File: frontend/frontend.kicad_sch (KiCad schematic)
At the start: 46 parts, among them Q1 T2N7002AK,LM, Q2 NX3008PBK,215, Q3 NX3008PBK,215, Q4 T2N7002AK,LM, Q5 NX3008PBK,215, Q6 T2N7002AK,LM, U1 ADS1291/2, U2 KC2016Z2

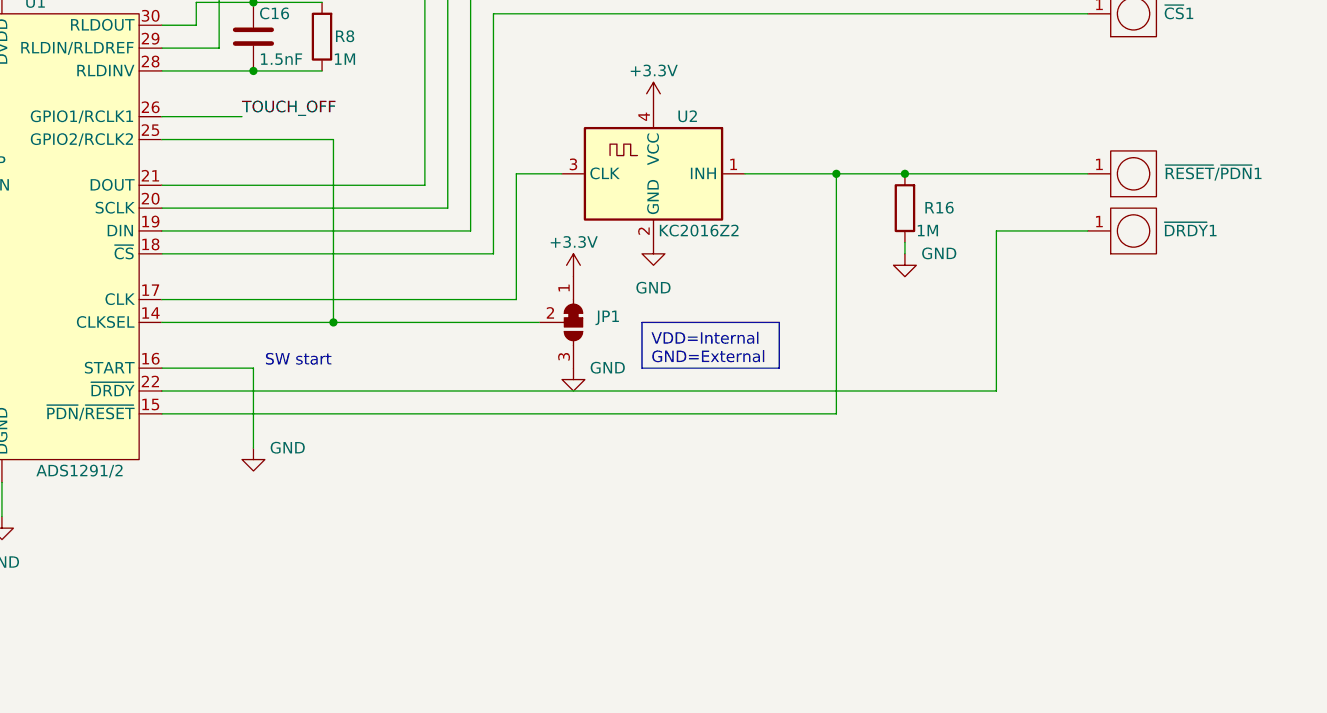
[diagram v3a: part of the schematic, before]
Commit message: Fix #8: add input to disable oscillator
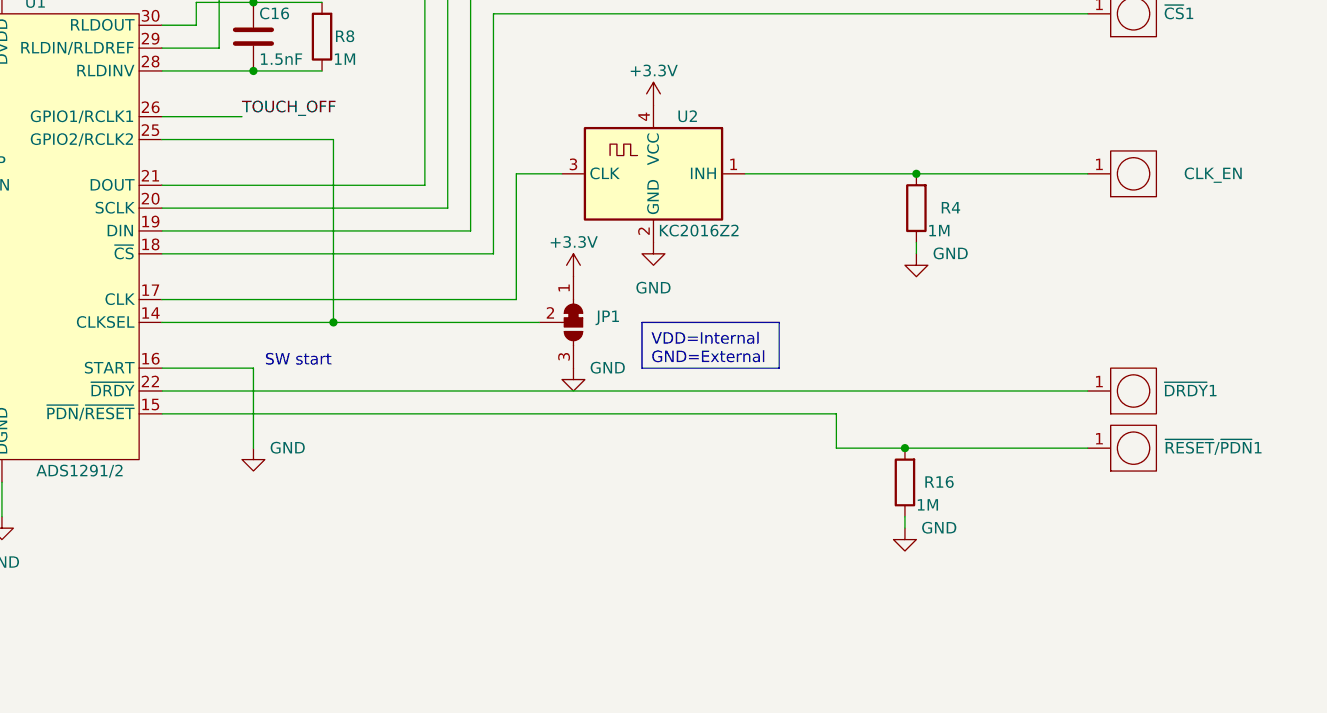
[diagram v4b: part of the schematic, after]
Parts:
- added CLK_EN: ~, frontend_parts:PAD, symbol frontend_parts:PAD
- added R4: 1M, Resistor_SMD:R_0603_1608Metric, symbol Device:R
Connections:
- net GND: now also R4.1
- net at R16.2, U1.15 (~{PDN}/~{RESET}), ~{RESET}/~{PDN}1.1: no longer U2.1 (INH)
- new net: CLK_EN.1, R4.2, U2.1 (INH)
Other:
- moved on the sheet: R16, ~{DRDY}1, ~{RESET}/~{PDN}1
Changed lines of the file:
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@@
   (junction (at 50.8 21.59) (diameter 0) (color 0 0 0 0)
   )
+  (junction (at 245.11 115.57) (diameter 0) (color 0 0 0 0)
+  )
   (junction (at 73.66 35.56) (diameter 0) (color 0 0 0 0)
   )
@@
   (junction (at 171.45 96.52) (diameter 0) (color 0 0 0 0)
   )
-  (junction (at 243.84 115.57) (diameter 0) (color 0 0 0 0)
-  )
   (junction (at 171.45 104.14) (diameter 0) (color 0 0 0 0)
   )
-  (junction (at 236.22 115.57) (diameter 0) (color 0 0 0 0)
-  )
   (junction (at 121.92 106.68) (diameter 0) (color 0 0 0 0)
   )
   (junction (at 156.21 87.63) (diameter 0) (color 0 0 0 0)
   )
+  (junction (at 243.84 146.05) (diameter 0) (color 0 0 0 0)
+  )
   (junction (at 52.07 67.31) (diameter 0) (color 0 0 0 0)
   )
@@
     (stroke (width 0) (type default))
   )
+  (wire (pts (xy 226.06 115.57) (xy 245.11 115.57))
+    (stroke (width 0) (type default))
+  )
   (wire (pts (xy 39.37 72.39) (xy 44.45 72.39))
     (stroke (width 0) (type default))
   )
-  (wire (pts (xy 236.22 115.57) (xy 243.84 115.57))
+  (wire (pts (xy 236.22 146.05) (xy 243.84 146.05))
     (stroke (width 0) (type default))
   )
@@
     (stroke (width 0) (type default))
   )
-  (wire (pts (xy 254 139.7) (xy 254 121.92))
-    (stroke (width 0) (type default))
-  )
   (wire (pts (xy 24.13 66.04) (xy 31.75 66.04))
     (stroke (width 0) (type default))
@@
     (stroke (width 0) (type default))
   )
+  (wire (pts (xy 245.11 123.19) (xy 245.11 124.46))
+    (stroke (width 0) (type default))
+  )
   (wire (pts (xy 143.51 149.86) (xy 143.51 153.67))
     (stroke (width 0) (type default))
@@
     (stroke (width 0) (type default))
   )
-  (wire (pts (xy 243.84 115.57) (xy 264.16 115.57))
+  (wire (pts (xy 243.84 146.05) (xy 264.16 146.05))
     (stroke (width 0) (type default))
   )
@@
     (stroke (width 0) (type default))
   )
-  (wire (pts (xy 226.06 115.57) (xy 236.22 115.57))
-    (stroke (width 0) (type default))
-  )
   (wire (pts (xy 57.15 101.6) (xy 125.73 101.6))
     (stroke (width 0) (type default))
@@
     (stroke (width 0) (type default))
   )
-  (wire (pts (xy 236.22 115.57) (xy 236.22 142.24))
+  (wire (pts (xy 236.22 146.05) (xy 236.22 142.24))
     (stroke (width 0) (type default))
   )
@@
     (stroke (width 0) (type default))
   )
-  (wire (pts (xy 254 121.92) (xy 264.16 121.92))
-    (stroke (width 0) (type default))
-  )
   (wire (pts (xy 66.04 40.64) (xy 66.04 44.45))
     (stroke (width 0) (type default))
@@
     (stroke (width 0) (type default))
   )
+  (wire (pts (xy 245.11 115.57) (xy 264.16 115.57))
+    (stroke (width 0) (type default))
+  )
   (wire (pts (xy 55.88 99.06) (xy 125.73 99.06))
     (stroke (width 0) (type default))
@@
     (stroke (width 0) (type default))
   )
-  (wire (pts (xy 243.84 123.19) (xy 243.84 124.46))
+  (wire (pts (xy 243.84 153.67) (xy 243.84 154.94))
     (stroke (width 0) (type default))
   )
@@
     (stroke (width 0) (type default))
   )
-  (wire (pts (xy 161.29 139.7) (xy 254 139.7))
+  (wire (pts (xy 161.29 139.7) (xy 264.16 139.7))
     (stroke (width 0) (type default))
   )
@@
     )
   )
-  (symbol (lib_id "frontend_parts:PAD") (at 269.24 121.92 0) (mirror x) (unit 1)
-    (in_bom yes) (on_board yes) (dnp no)
-    (property "Reference" "~{DRDY}1" (at 275.59 121.92 0)
-      (effects (font (size 1.27 1.27)))
-    )
-    (property "Value" "~" (at 264.16 124.46 0)
-      (effects (font (size 1.27 1.27)))
-    )
-    (property "Footprint" "frontend_parts:PAD" (at 264.16 124.46 0)
-      (effects (font (size 1.27 1.27)) hide)
-    )
-    (property "Datasheet" "" (at 264.16 124.46 0)
+  (symbol (lib_id "frontend_parts:PAD") (at 269.24 139.7 0) (mirror x) (unit 1)
+    (in_bom yes) (on_board yes) (dnp no)
+    (property "Reference" "~{DRDY}1" (at 275.59 139.7 0)
+      (effects (font (size 1.27 1.27)))
+    )
+    (property "Value" "~" (at 264.16 142.24 0)
+      (effects (font (size 1.27 1.27)))
+    )
+    (property "Footprint" "frontend_parts:PAD" (at 264.16 142.24 0)
+      (effects (font (size 1.27 1.27)) hide)
+    )
+    (property "Datasheet" "" (at 264.16 142.24 0)
       (effects (font (size 1.27 1.27)) hide)
     )
@@
         (path "/e7afbd42-f5d0-401b-b125-21ade79cd152"
           (reference "R2") (unit 1)
+        )
+      )
+    )
+  )
+  (symbol (lib_id "frontend_parts:PAD") (at 269.24 115.57 0) (mirror x) (unit 1)
+    (in_bom yes) (on_board yes) (dnp no)
+    (property "Reference" "CLK_EN" (at 278.13 115.57 0)
+      (effects (font (size 1.27 1.27)))
+    )
+    (property "Value" "~" (at 264.16 118.11 0)
+      (effects (font (size 1.27 1.27)))
+    )
+    (property "Footprint" "frontend_parts:PAD" (at 264.16 118.11 0)
+      (effects (font (size 1.27 1.27)) hide)
+    )
+    (property "Datasheet" "" (at 264.16 118.11 0)
+      (effects (font (size 1.27 1.27)) hide)
+    )
+    (pin "1")
+    (instances
+      (project "frontend"
+        (path "/e7afbd42-f5d0-401b-b125-21ade79cd152"
+          (reference "CLK_EN") (unit 1)
         )
       )
@@
     )
   )
-  (symbol (lib_id "frontend_parts:PAD") (at 269.24 115.57 0) (mirror x) (unit 1)
-    (in_bom yes) (on_board yes) (dnp no)
-    (property "Reference" "~{RESET}/~{PDN}1" (at 278.13 115.57 0)
-      (effects (font (size 1.27 1.27)))
-    )
-    (property "Value" "~" (at 264.16 118.11 0)
-      (effects (font (size 1.27 1.27)))
-    )
-    (property "Footprint" "frontend_parts:PAD" (at 264.16 118.11 0)
-      (effects (font (size 1.27 1.27)) hide)
-    )
-    (property "Datasheet" "" (at 264.16 118.11 0)
+  (symbol (lib_id "frontend_parts:PAD") (at 269.24 146.05 0) (mirror x) (unit 1)
+    (in_bom yes) (on_board yes) (dnp no)
+    (property "Reference" "~{RESET}/~{PDN}1" (at 278.13 146.05 0)
+      (effects (font (size 1.27 1.27)))
+    )
+    (property "Value" "~" (at 264.16 148.59 0)
+      (effects (font (size 1.27 1.27)))
+    )
+    (property "Footprint" "frontend_parts:PAD" (at 264.16 148.59 0)
+      (effects (font (size 1.27 1.27)) hide)
+    )
+    (property "Datasheet" "" (at 264.16 148.59 0)
       (effects (font (size 1.27 1.27)) hide)
     )
@@
     )
   )
-  (symbol (lib_id "Device:R") (at 243.84 119.38 180) (unit 1)
-    (in_bom yes) (on_board yes) (dnp no)
-    (property "Reference" "R16" (at 247.65 119.38 0)
-      (effects (font (size 1.27 1.27)))
-    )
-    (property "Value" "1M" (at 246.38 121.92 0)
-      (effects (font (size 1.27 1.27)))
-    )
-    (property "Footprint" "Resistor_SMD:R_0603_1608Metric" (at 245.618 119.38 90)
-      (effects (font (size 1.27 1.27)) hide)
-    )
-    (property "Datasheet" "~" (at 243.84 119.38 0)
+  (symbol (lib_id "Device:R") (at 243.84 149.86 180) (unit 1)
+    (in_bom yes) (on_board yes) (dnp no)
+    (property "Reference" "R16" (at 247.65 149.86 0)
+      (effects (font (size 1.27 1.27)))
+    )
+    (property "Value" "1M" (at 246.38 152.4 0)
+      (effects (font (size 1.27 1.27)))
+    )
+    (property "Footprint" "Resistor_SMD:R_0603_1608Metric" (at 245.618 149.86 90)
+      (effects (font (size 1.27 1.27)) hide)
+    )
+    (property "Datasheet" "~" (at 243.84 149.86 0)
       (effects (font (size 1.27 1.27)) hide)
     )
@@
     )
   )
-  (symbol (lib_id "power:GND") (at 243.84 124.46 0) (unit 1)
-    (in_bom yes) (on_board yes) (dnp no)
-    (property "Reference" "#PWR025" (at 243.84 130.81 0)
-      (effects (font (size 1.27 1.27)) hide)
-    )
-    (property "Value" "GND" (at 247.65 124.46 0)
-      (effects (font (size 1.27 1.27)))
-    )
-    (property "Footprint" "" (at 243.84 124.46 0)
-      (effects (font (size 1.27 1.27)) hide)
-    )
-    (property "Datasheet" "" (at 243.84 124.46 0)
+  (symbol (lib_id "power:GND") (at 243.84 154.94 0) (unit 1)
+    (in_bom yes) (on_board yes) (dnp no)
+    (property "Reference" "#PWR025" (at 243.84 161.29 0)
+      (effects (font (size 1.27 1.27)) hide)
+    )
+    (property "Value" "GND" (at 247.65 154.94 0)
+      (effects (font (size 1.27 1.27)))
+    )
+    (property "Footprint" "" (at 243.84 154.94 0)
+      (effects (font (size 1.27 1.27)) hide)
+    )
+    (property "Datasheet" "" (at 243.84 154.94 0)
       (effects (font (size 1.27 1.27)) hide)
     )
@@
     )
   )
+  (symbol (lib_id "power:GND") (at 245.11 124.46 0) (unit 1)
+    (in_bom yes) (on_board yes) (dnp no)
+    (property "Reference" "#PWR022" (at 245.11 130.81 0)
+      (effects (font (size 1.27 1.27)) hide)
+    )
+    (property "Value" "GND" (at 248.92 124.46 0)
+      (effects (font (size 1.27 1.27)))
+    )
+    (property "Footprint" "" (at 245.11 124.46 0)
+      (effects (font (size 1.27 1.27)) hide)
+    )
+    (property "Datasheet" "" (at 245.11 124.46 0)
+      (effects (font (size 1.27 1.27)) hide)
+    )
+    (pin "1")
+    (instances
+      (project "frontend"
+        (path "/e7afbd42-f5d0-401b-b125-21ade79cd152"
+          (reference "#PWR022") (unit 1)
+        )
+      )
+    )
+  )
   (symbol (lib_id "power:GNDA") (at 100.33 149.86 0) (unit 1)
     (in_bom yes) (on_board yes) (dnp no) (fields_autoplaced)
@@
         )
       )
+    )
+  )
+  (symbol (lib_id "Device:R") (at 245.11 119.38 180) (unit 1)
+    (in_bom yes) (on_board yes) (dnp no)
+    (property "Reference" "R4" (at 248.92 119.38 0)
+      (effects (font (size 1.27 1.27)))
+    )
+    (property "Value" "1M" (at 247.65 121.92 0)
+      (effects (font (size 1.27 1.27)))
+    )
+    (property "Footprint" "Resistor_SMD:R_0603_1608Metric" (at 246.888 119.38 90)
+      (effects (font (size 1.27 1.27)) hide)
+    )
+    (property "Datasheet" "~" (at 245.11 119.38 0)
+      (effects (font (size 1.27 1.27)) hide)
+    )
+    (pin "1")
+    (pin "2")
+    (instances
+      (project "frontend"
+        (path "/e7afbd42-f5d0-401b-b125-21ade79cd152"
+          (reference "R4") (unit 1)
+        )
+      )

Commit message: Update frontend layout
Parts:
- renumbered CLK_EN to CLK_EN1
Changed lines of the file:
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@@
   (title_block
     (title "Card/IO ECG daughter board")
-    (date "2023-04-25")
-    (rev "1")
+    (date "2023-05-19")
+    (rev "2")
   )
   (junction (at 129.54 80.01) (diameter 0) (color 0 0 0 0)
@@
   (symbol (lib_id "frontend_parts:PAD") (at 269.24 115.57 0) (mirror x) (unit 1)
     (in_bom yes) (on_board yes) (dnp no)
-    (property "Reference" "CLK_EN" (at 278.13 115.57 0)
+    (property "Reference" "CLK_EN1" (at 278.13 115.57 0)
       (effects (font (size 1.27 1.27)))
     )
@@
       (project "frontend"
         (path "/e7afbd42-f5d0-401b-b125-21ade79cd152"
-          (reference "CLK_EN") (unit 1)
+          (reference "CLK_EN1") (unit 1)
         )
       )

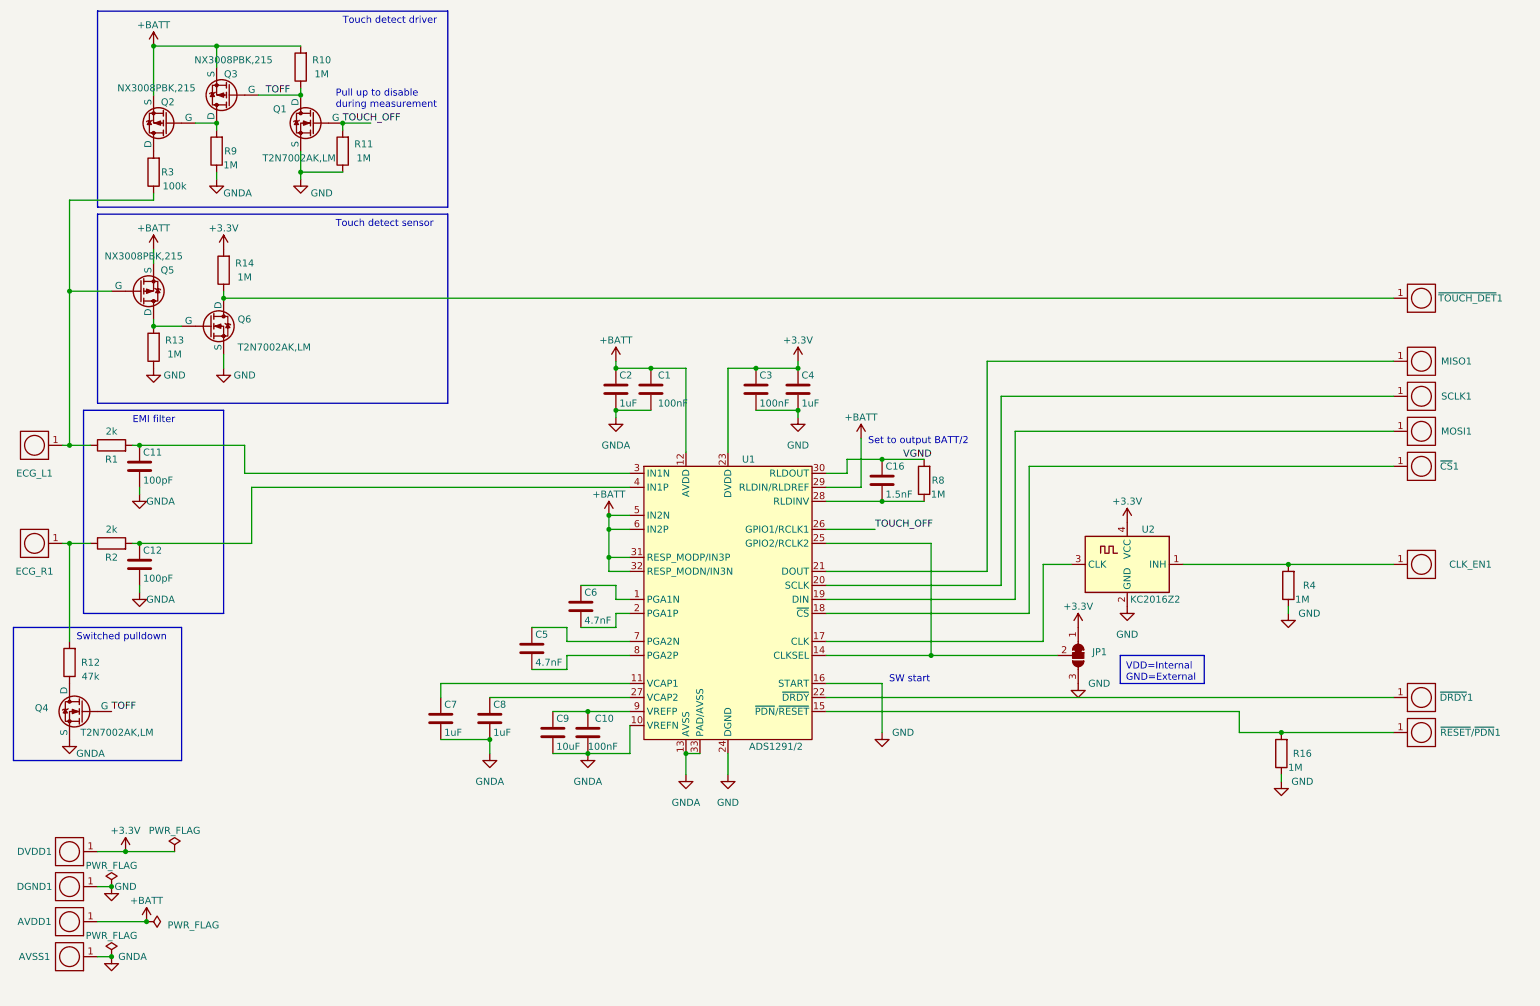
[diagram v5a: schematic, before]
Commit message: Fix #18: add RLD output, fix main board revision
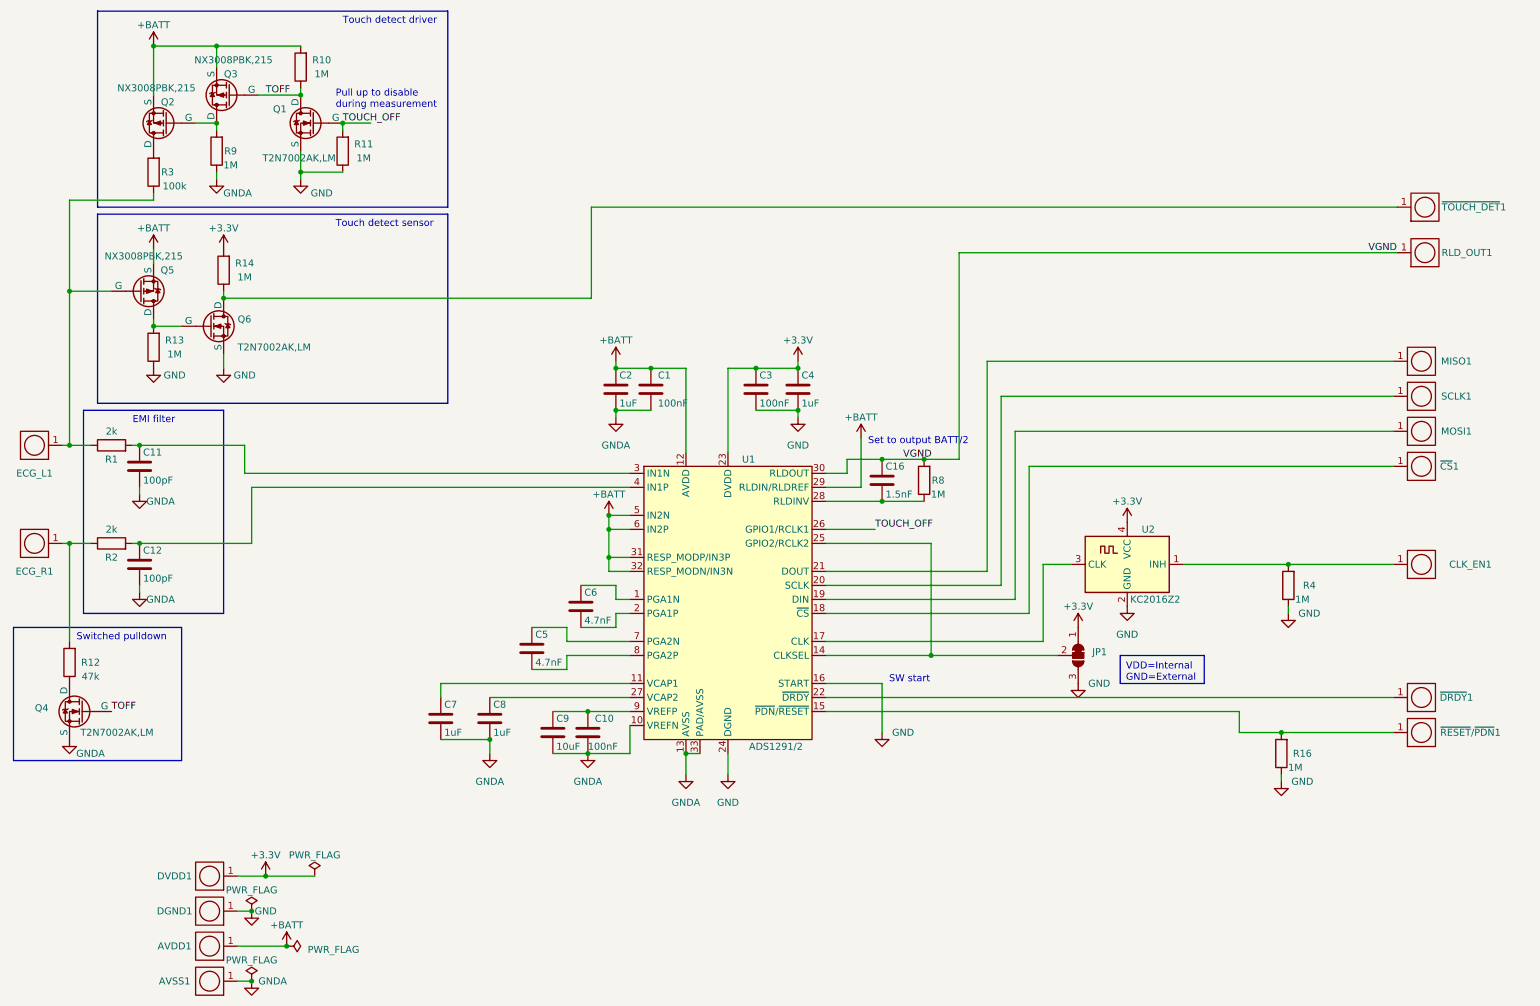
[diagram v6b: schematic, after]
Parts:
- added RLD_OUT1: ~, frontend_parts:PAD, symbol frontend_parts:PAD
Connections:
- net VGND: now also RLD_OUT1.1
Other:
- moved on the sheet: AVDD1, AVSS1, DGND1, DVDD1, ~{TOUCH_DET}1
